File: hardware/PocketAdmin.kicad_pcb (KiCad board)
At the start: 2 copper layers, 15 x 31 mm, 21 parts, among them CON1 ST-LINK_V2, J1 USB_A_Plug, SW1 TL3342, U1 IP4220CZ6, U2 MCP1700-3302E_SOT23, U3 STM32F072C8Tx, U4 W25Q256FVFG, Y1 8MHz

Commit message: first testing release of 1.3 revision
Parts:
- added C12: 100nF, Capacitor_SMD:C_0603_1608Metric, F.Cu at (131.6, 94.6)
- added D1: GREEN, LED_SMD:LED_0603_1608Metric, F.Cu at (141.7, 85.9)
- added R3: 4.7k, Resistor_SMD:R_0603_1608Metric, F.Cu at (142.7, 94.6)
- added R4: 4.7k, Resistor_SMD:R_0603_1608Metric, F.Cu at (141.7, 82.1)
- U2: value MCP1700-3302E_SOT23 -> MCP1700-3302E/TT
- U4: value W25Q256FVFG -> W25N01GVZEIG; footprint Package_SO:SOIC-16W_7.5x10.3mm_P1.27mm -> PocketAdmin:WSON-8_8x6mm
- moved U4 5.88 mm to (139.4, 80.7), turned to 270 degrees
- moved C9 4.03 mm to (138.7, 91.2), turned to 180 degrees
- moved C10 3.79 mm to (135.4, 91.2), turned to 180 degrees
- moved C7 1.05 mm to (142.2, 92.7)
- moved C11 0.50 mm to (142.2, 94.4)
- moved C8 0.41 mm to (132.3, 93.4)
- moved C4 0.40 mm to (142.2, 96.5)
- moved C5 0.40 mm to (132.8, 96.5)
- moved Y1 0.40 mm to (137.5, 95.6)
- moved SW1 0.15 mm to (137.1, 94.8)
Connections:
- CON1 pad 5: Net-(CON1-Pad5) -> boot0
- U3 pad 13: Net-(U3-Pad13) -> hold
- U3 pad 19: Net-(U3-Pad19) -> cs
- U3 pad 21: Net-(U3-Pad21) -> miso
- U3 pad 22: Net-(U3-Pad22) -> wp
- U3 pad 38: cs -> Net-(U3-Pad38)
- U3 pad 44: GND -> boot0
- U4 pad 1: 3.3V -> cs
- U4 pad 2: 3.3V -> miso
- U4 pad 3: nrst -> wp
- U4 pad 4: Net-(U4-Pad11) -> GND
- U4 pad 5: Net-(U4-Pad11) -> mosi
- U4 pad 6: Net-(U4-Pad11) -> sck
- U4 pad 7: cs -> hold
- U4 pad 8: miso -> 3.3V
- U4 pad 9: 3.3V -> GND
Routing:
- net boot0: track 0.00 -> 34.2 mm, vias 0 -> 2
- net wp: track 0.00 -> 10.4 mm, vias 0 -> 1
- net hold: track 0.00 -> 9.82 mm, vias 0 -> 1
- net cs: track 5.69 -> 13.8 mm
- net nrst: track 13.9 -> 8.81 mm, vias 1 -> 0
- net sck: track 3.91 -> 7.36 mm
- net Net-(D1-Pad2): track 0.00 -> 2.99 mm, vias 0 -> 1
- net GND: track 9.76 -> 7.12 mm, vias 9 -> 10
- net Net-(C10-Pad2): track 6.63 -> 4.12 mm
- net Net-(D1-Pad1): track 0.00 -> 2.26 mm
- net mosi: track 3.82 -> 5.97 mm
- net Net-(C5-Pad1): track 7.45 -> 9.15 mm
- net Net-(C4-Pad1): track 7.45 -> 9.15 mm
- net miso: track 17.9 -> 16.4 mm
- net 3.3V: track 80.4 -> 79.5 mm, vias 2 -> 1
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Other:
- board text added: "rev_1.3"
- board text removed: "rev_1.2"

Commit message: changed NRST capacitor
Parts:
- C11: value 18pF -> 100nF
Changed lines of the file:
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@@
-(kicad_pcb (version 20171130) (host pcbnew 5.1.5+dfsg1-2)
+(kicad_pcb (version 20171130) (host pcbnew 5.0.2+dfsg1-1)
   (general
     (thickness 1.6)
@@
     (zone_45_only no)
     (trace_min 0.19)
+    (segment_width 0.2)
+    (edge_width 0.15)
     (via_size 0.6)
     (via_drill 0.4)
@@
     (uvia_min_size 0.2)
     (uvia_min_drill 0.1)
-    (edge_width 0.15)
-    (segment_width 0.2)
     (pcb_text_width 0.3)
     (pcb_text_size 1.5 1.5)
@@
       (effects (font (size 1 1) (thickness 0.15)) (justify mirror))
     )
-    (fp_text value 18pF (at 0 -1.43) (layer B.Fab)
-      (effects (font (size 1 1) (thickness 0.15)) (justify mirror))
-    )
+    (fp_text value 100nF (at 0 -1.43) (layer B.Fab)
+      (effects (font (size 1 1) (thickness 0.15)) (justify mirror))
+    )

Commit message: move to newer toolchain versions
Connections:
- U3 pad 10: Net-(U3-Pad10) -> unconnected-(U3-Pad10)
- U3 pad 11: Net-(U3-Pad11) -> unconnected-(U3-Pad11)
- U3 pad 14: Net-(U3-Pad14) -> unconnected-(U3-Pad14)
- U3 pad 18: Net-(U3-Pad18) -> unconnected-(U3-Pad18)
- U3 pad 20: Net-(U3-Pad20) -> unconnected-(U3-Pad20)
- U3 pad 25: Net-(U3-Pad25) -> unconnected-(U3-Pad25)
- U3 pad 27: Net-(U3-Pad27) -> unconnected-(U3-Pad27)
- U3 pad 29: Net-(U3-Pad29) -> unconnected-(U3-Pad29)
- U3 pad 3: Net-(U3-Pad3) -> unconnected-(U3-Pad3)
- U3 pad 31: Net-(U3-Pad31) -> unconnected-(U3-Pad31)
- U3 pad 38: Net-(U3-Pad38) -> unconnected-(U3-Pad38)
- U3 pad 40: Net-(U3-Pad40) -> unconnected-(U3-Pad40)
- U3 pad 42: Net-(U3-Pad42) -> unconnected-(U3-Pad42)
- U3 pad 45: Net-(U3-Pad45) -> unconnected-(U3-Pad45)
- U3 pad 46: Net-(U3-Pad46) -> unconnected-(U3-Pad46)
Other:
- net class Default removed

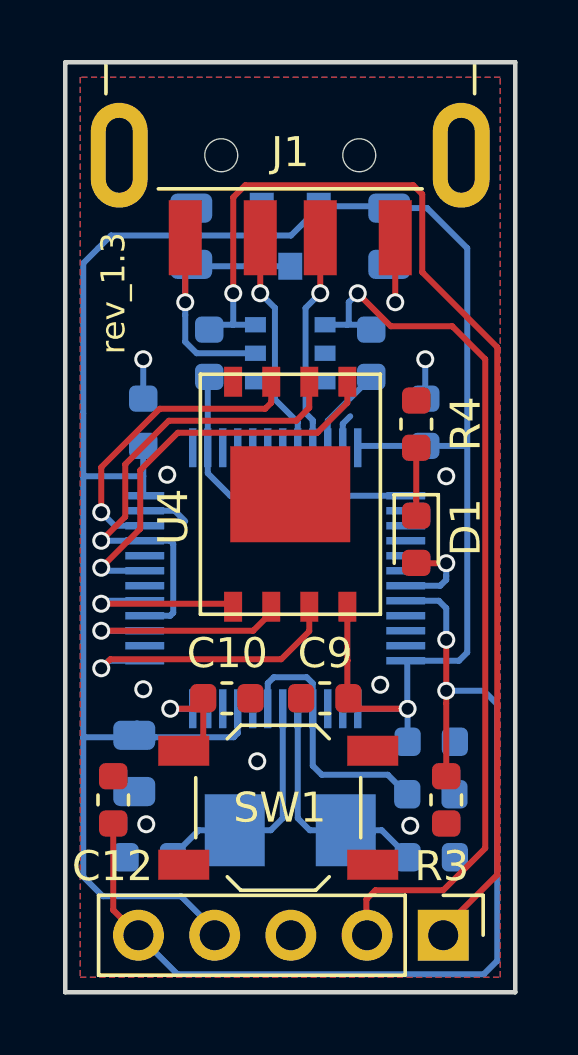
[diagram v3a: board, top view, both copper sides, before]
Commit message: tiny PCB change to simplify manufacturing
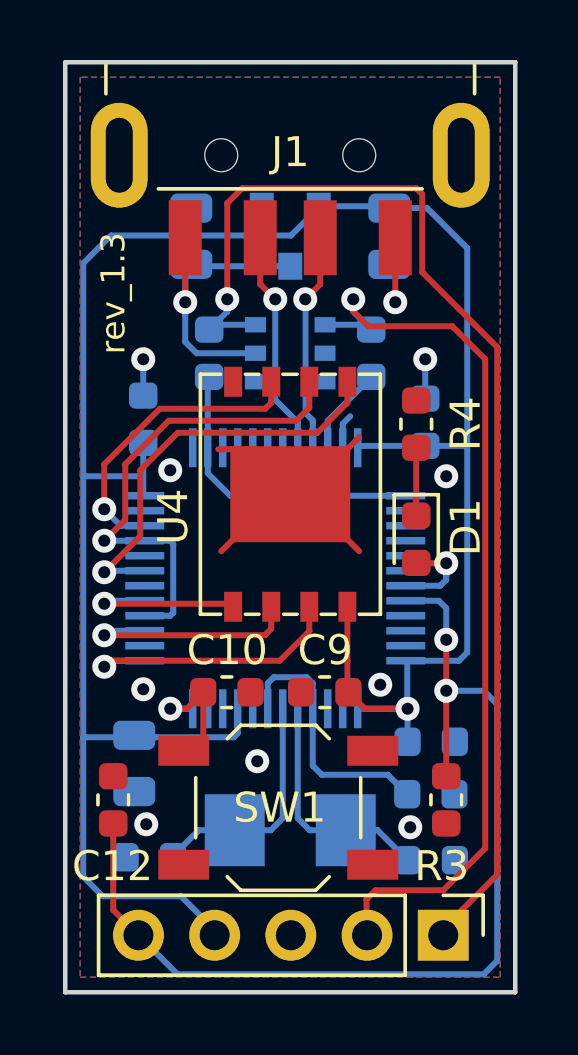
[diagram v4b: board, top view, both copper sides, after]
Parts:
- moved C10 0.20 mm to (135.4, 91.0)
- moved C9 0.20 mm to (138.7, 91.0)
- moved C4 0.10 mm to (142.2, 96.6)
- moved C6 0.10 mm to (132.6, 81.9)
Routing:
- net GND: track 7.12 -> 17.9 mm
- net swclk: track 38.7 -> 39.2 mm
